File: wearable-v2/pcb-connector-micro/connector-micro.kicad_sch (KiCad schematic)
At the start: 44 parts, among them J1 HERALD_V2_CONN_RECEPTACLE, J10 Conn_01x01_Pin, J11 PNL_1, J12 PNL_2, J13 PNL_3, J14 PNL_4, J15 Conn_01x01_Pin, J16 Conn_01x01_Pin, J17 Conn_01x01_Pin, J18 Conn_01x02_Pin, J2 HERALD_V2_CONN_RECEPTACLE, J3 HERALD_V2_CONN_RECEPTACLE, J4 HERALD_V2_CONN_RECEPTACLE, J5 Conn_01x01_Pin, J6 Conn_01x01_Pin, J7 USB_C_Receptacle_USB2.0, J8 Conn_01x01_Pin, J9 Conn_01x01_Pin, SW1 PTS526, U1 DT1446-04V, U15 TLV751, U2 MCP73831/2-2MC, U3 TCA6408A, U4 FT201XQ

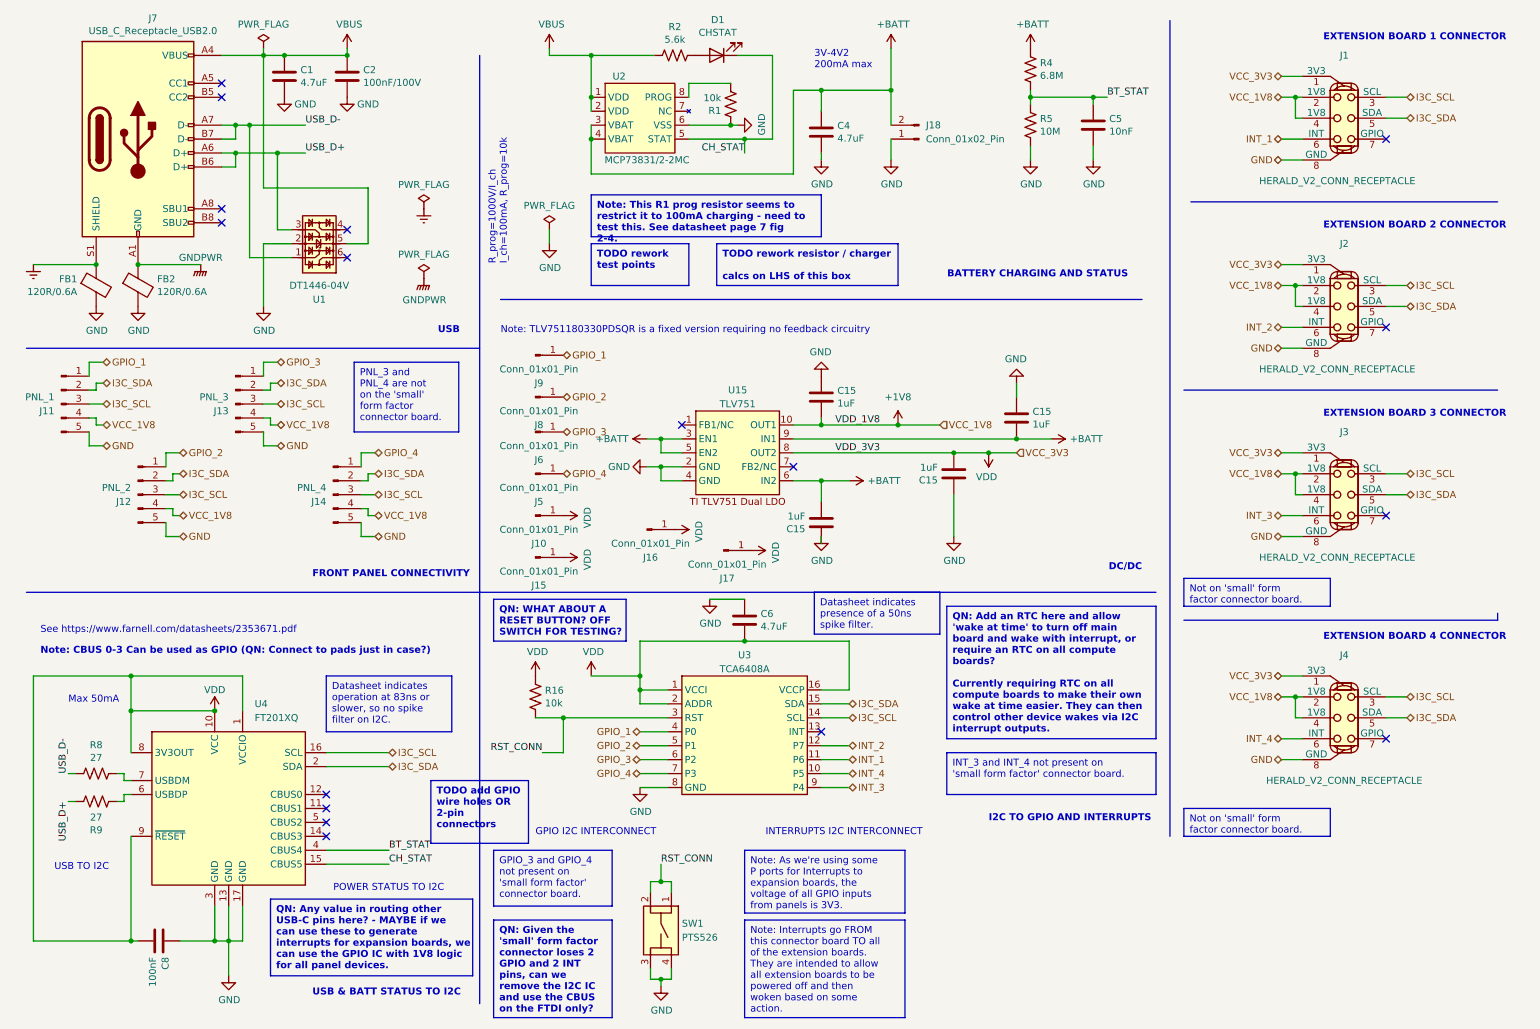
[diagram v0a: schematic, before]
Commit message: Added Antenna panel and Micro connector boards
Micro connector uses the nPM1300 PMIC from Nordic Semi.
Signed-off-by: Adam Fowler <adam@adamfowler.org>
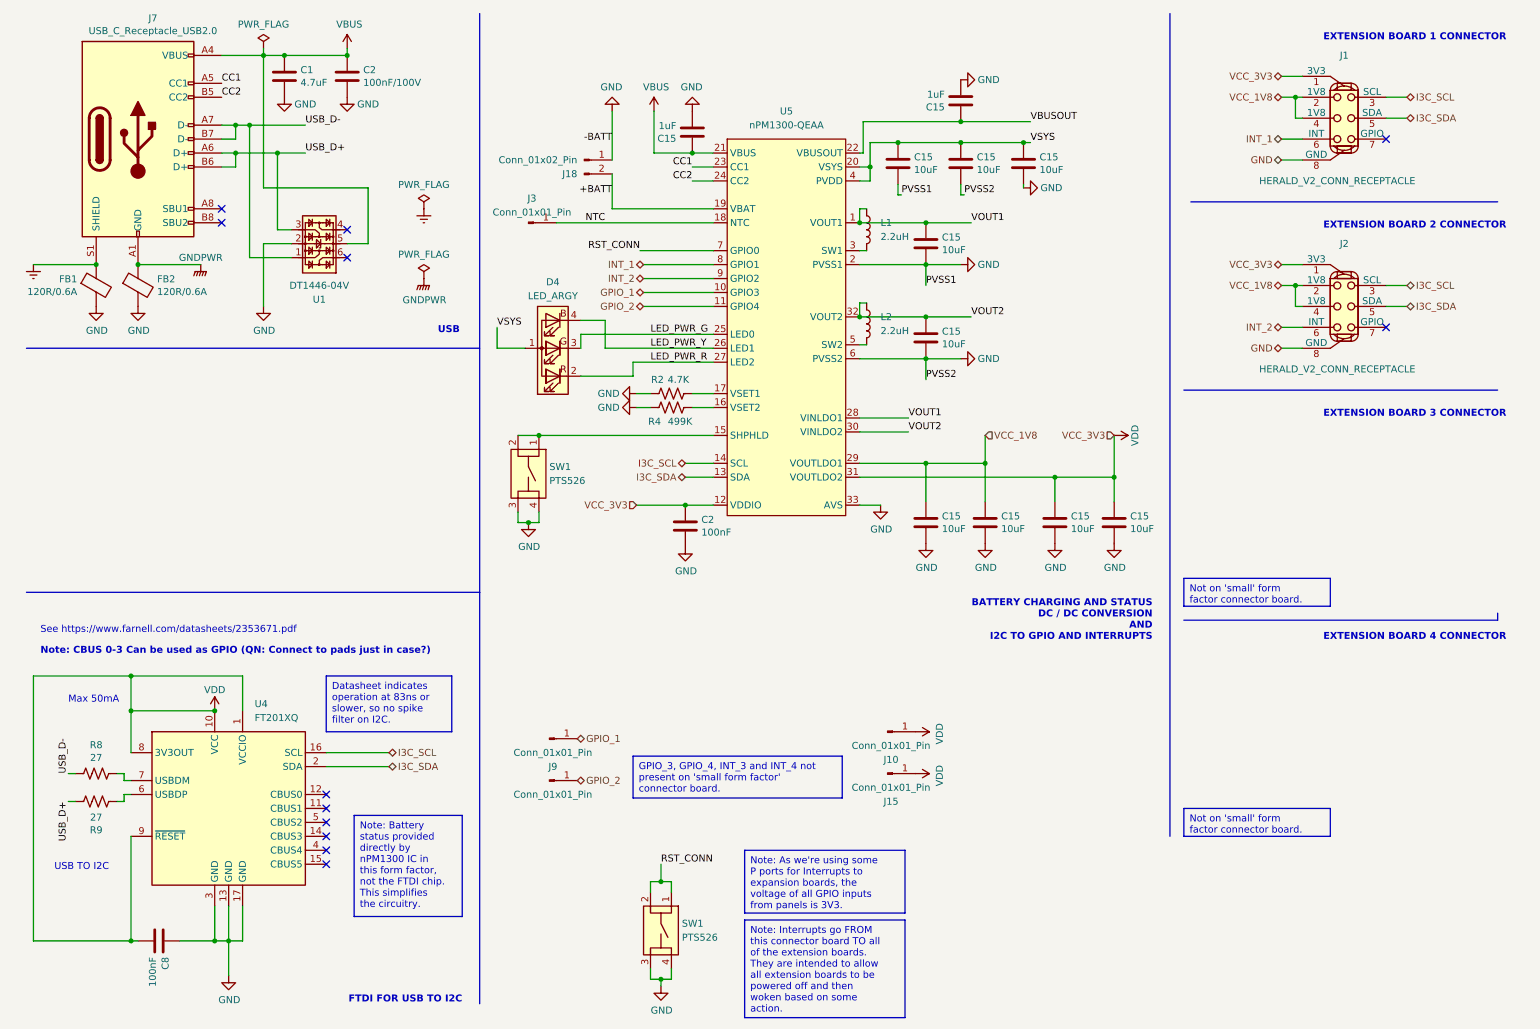
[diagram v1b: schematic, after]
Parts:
- removed C15 (x4): 1uF, Capacitor_SMD:C_0402_1005Metric, symbol Device:C
- removed C4, C6: 4.7uF, Capacitor_SMD:C_0402_1005Metric, symbol Device:C
- removed C5: 10nF, Capacitor_SMD:C_0402_1005Metric, symbol Device:C
- removed D1: CHSTAT, LED_SMD:LED_0603_1608Metric, symbol Device:LED
- removed J11: PNL_1, symbol Connector:Conn_01x05_Pin
- removed J12: PNL_2, symbol Connector:Conn_01x05_Pin
- removed J13: PNL_3, symbol Connector:Conn_01x05_Pin
- removed J14: PNL_4, symbol Connector:Conn_01x05_Pin
- removed J16, J17, J5, J6: Conn_01x01_Pin, Connector_PinHeader_1.00mm:PinHeader_1x01_P1.00mm_Vertical, symbol Connector:Conn_01x01_Pin
- removed J3, J4: HERALD_V2_CONN_RECEPTACLE, Herald:HERALD_V2_CONN_RECEPTACLE, symbol Herald_Extras:HERALD_V2_CONN_RECEPTACLE
- removed R1, R16: 10k, Resistor_SMD:R_0402_1005Metric, symbol Device:R_US
- removed R5: 10M, Resistor_SMD:R_0402_1005Metric, symbol Device:R_US
- removed U15: TLV751, Herald:SON40P200X200X80-11N, symbol Herald:TLV751
- removed U2: MCP73831/2-2MC, Package_DFN_QFN:DFN-8-1EP_3x2mm_P0.5mm_EP1.75x1.45mm, symbol Herald_Extras:MCP73831/2-2MC
- removed U3: TCA6408A, Herald:QFN40P180X260X55-16N, symbol Herald_Extras:TCA6408A
- added C15 (x9): 10uF, Capacitor_SMD:C_0402_1005Metric, symbol Device:C
- added C15 (x2): 1uF, Capacitor_SMD:C_0402_1005Metric, symbol Device:C
- added C2: 100nF, Capacitor_SMD:C_0402_1005Metric, symbol Device:C
- added D4: LED_ARGY, Herald:LED_Kingbright_APHF1608, symbol Device:LED_ARGB
- added J3: Conn_01x01_Pin, Connector_PinHeader_1.00mm:PinHeader_1x01_P1.00mm_Vertical, symbol Connector:Conn_01x01_Pin
- added L1, L2: 2.2uH, Inductor_SMD:L_1008_2520Metric, symbol Device:L
- added SW1: PTS526, Herald:PTS526, symbol Herald_Extras:SPST_NO_RESET
- added U5: nPM1300-QEAA, Package_DFN_QFN:QFN-32-1EP_5x5mm_P0.5mm_EP3.6x3.6mm, symbol Herald_Extras:nPM1300
- R2: value 5.6k -> 4.7K; MPN RC0402FR-075R6L -> RC0402FR-074K7L
- R4: value 6.8M -> 499K; MPN RK73H1ETTP6804F -> RK73H1ETTP4993F
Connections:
- net +BATT: now also U5.19 (VBAT); no longer R4.1
- net GND: now also R2.2, R4.1, C15.2, C15.2, C15.2, C15.2, C15.2, C15.2, C15.2, C15.2, C15.2, C15.2, C15.2, C2.1, SW1.3, SW1.4, U5.2 (PVSS1), U5.33 (AVS), U5.6 (PVSS2)
- net GPIO_1: now also U5.10 (GPIO3)
- net GPIO_2: now also U5.11 (GPIO4)
- net I3C_SCL: now also U5.14 (SCL)
- net I3C_SDA: now also U5.13 (SDA)
- net INT_1: now also U5.8 (GPIO1)
- net INT_2: now also U5.9 (GPIO2)
- net RST_CONN: now also U5.7 (GPIO0)
- net VBUS: now also C15.1, U5.21 (VBUS); no longer R2.2
- net VDD: now also C15.1, C15.1, C2.2, U5.12 (VDDIO), U5.31 (VOUTLDO2)
- net CC1: now reaches J7.A5 (CC1)
- net CC1: now also U5.23 (CC1)
- net CC2: now reaches J7.B5 (CC2)
- net CC2: now also U5.24 (CC2)
- net at R2.1: now also U5.17 (VSET1)
- net +1V8 renamed VCC_1V8
- net VCC_1V8: now also C15.1, C15.1, U5.29 (VOUTLDO1)
- net BT_STAT: no longer names the net of U4.4 (CBUS4)
- net BT_STAT: no longer R4.2
- net CH_STAT: no longer names the net of U4.15 (CBUS5)
- new net: L1.2, U5.3 (SW1)
- new net: SW1.1, SW1.2, U5.15 (SHPHLD)
- new net: R4.2, U5.16 (VSET2)
- new net: L2.2, U5.5 (SW2)
- new net LED_PWR_G: D4.3 (GK), U5.25 (LED0)
- new net LED_PWR_R: D4.2 (RK), U5.27 (LED2)
- new net LED_PWR_Y: D4.4 (BK), U5.26 (LED1)
- new net NTC: J3.1 (Pin_1), U5.18 (NTC)
- new net VBUSOUT: C15.1, U5.22 (VBUSOUT)
- new net VOUT1: C15.1, L1.1, U5.1 (VOUT1), U5.28 (VINLDO1)
- new net VOUT2: C15.1, L2.1, U5.30 (VINLDO2), U5.32 (VOUT2)
- new net VSYS: C15.1, C15.1, C15.1, D4.1 (A), U5.20 (VSYS), U5.4 (PVDD)
- no-connect marks 17 -> 12
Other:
- note added: "BATTERY CHARGING AND STATUS DC / DC CONVERSION AND I2C TO GPIO AND INTERRUPTS"
- note added: "FTDI FOR USB TO I2C"
- note removed: "3V-4V2 200mA max"
- note removed: "BATTERY CHARGING AND STATUS"
- note removed: "DC/DC"
- note removed: "FRONT PANEL CONNECTIVITY"
- note removed: "GPIO I2C INTERCONNECT"
- note removed: "I2C TO GPIO AND INTERRUPTS"
- note removed: "INTERRUPTS I2C INTERCONNECT"
- note removed: "Note: TLV751180330PDSQR is a fixed version requiring no feedback circuitry"
- note removed: "POWER STATUS TO I2C"
- note removed: "R_prog=1000V/I_ch I_ch=100mA, R_prog=10k"
- note removed: "USB & BATT STATUS TO I2C"
- moved on the sheet: J10, J15, J9
